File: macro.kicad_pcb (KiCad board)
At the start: 2 copper layers, 87.7 x 40.5 mm, 62 parts, among them J1 Conn_01x01_Male, J2 Conn_01x01_Male, J3 Conn_01x01_Male, Q1 BSS138, SW1 RotaryEncoder_Switch, SW2 SW_Push, U1 AP2112K-3.3, U2 W25Q128JVPIQ, U3 RP2040, Y1 12MHz

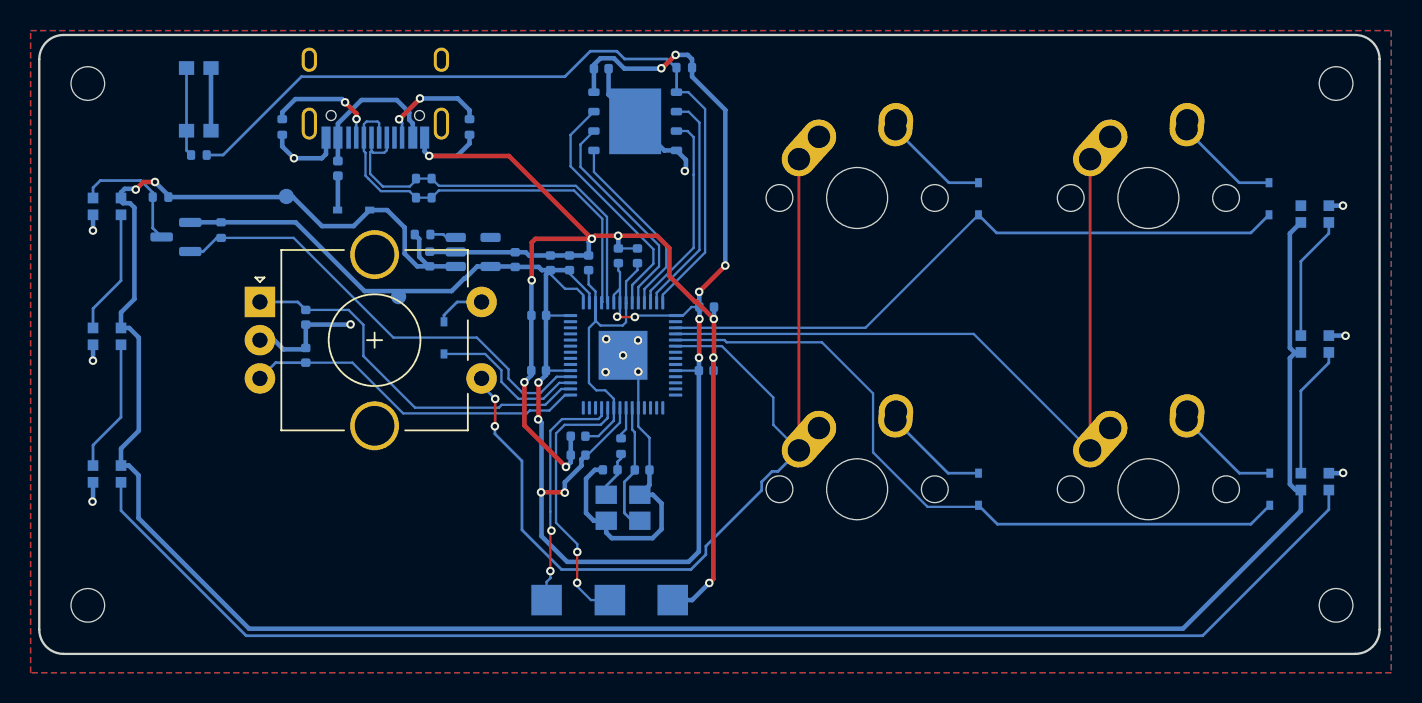
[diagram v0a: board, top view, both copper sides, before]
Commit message: Add tooling holes and logo
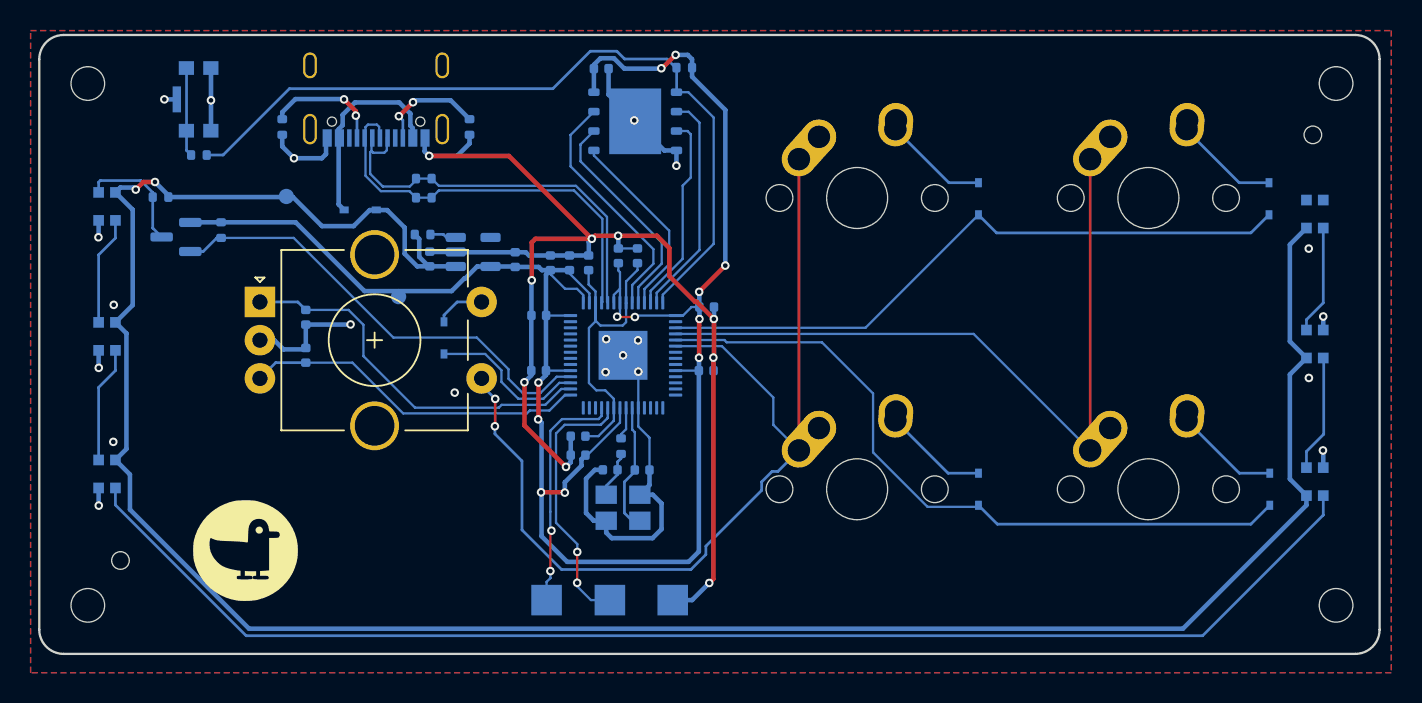
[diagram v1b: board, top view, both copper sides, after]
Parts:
- removed F1: Polyfuse, Fuse:Fuse_0402_1005Metric
- added G***: LOGO, duck:bg, F.Cu at (119.1, 111.5)
- added REF**: Tooling_Hole, MountingHole:Tooling_Hole, F.Cu at (188.9, 84.3)
- added REF**: Tooling_Hole, MountingHole:Tooling_Hole, F.Cu at (110.9, 112.2)
- SW2: footprint Button_Switch_SMD:SW_Push_1P1T_NO_CK_KMR2 -> KMR221GLFS:SW_KMR221GLFS
- USB1: footprint Type-C:HRO-TYPE-C-31-M-12-Assembly -> TYPE-C-31-M-12:HRO_TYPE-C-31-M-12
- moved USB1 4.05 mm to (127.6, 80.8)
- moved D1 0.43 mm to (126.6, 89.2)
- turned D10 to -90 degrees
- turned D11 to -90 degrees
- turned D12 to -90 degrees
- turned D7 to 90 degrees
- turned D8 to 90 degrees
- turned D9 to 90 degrees
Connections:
- D1 pad 2: Net-(D1-Pad2) -> VBUS
- D10 pad 1: +5V -> unconnected-(D10-Pad1)
- D10 pad 2: unconnected-(D10-Pad2) -> GND
- D10 pad 3: GND -> Net-(D10-Pad3)
- D10 pad 4: Net-(D10-Pad4) -> +5V
- D11 pad 1: +5V -> Net-(D10-Pad3)
- D11 pad 2: Net-(D10-Pad4) -> GND
- D11 pad 3: GND -> Net-(D11-Pad3)
- D11 pad 4: Net-(D11-Pad4) -> +5V
- D12 pad 1: +5V -> Net-(D11-Pad3)
- D12 pad 2: Net-(D11-Pad4) -> GND
- D12 pad 3: GND -> Net-(D12-Pad3)
- D12 pad 4: Net-(D12-Pad4) -> +5V
- D7 pad 1: +5V -> Net-(D7-Pad1)
- D7 pad 2: Net-(D7-Pad2) -> GND
- D7 pad 3: GND -> LED_DIN_5V
- D7 pad 4: LED_DIN_5V -> +5V
- D8 pad 1: +5V -> Net-(D8-Pad1)
- D8 pad 2: Net-(D8-Pad2) -> GND
- D8 pad 3: GND -> Net-(D7-Pad1)
- D8 pad 4: Net-(D7-Pad2) -> +5V
- D9 pad 1: +5V -> Net-(D12-Pad3)
- D9 pad 2: Net-(D12-Pad4) -> GND
- D9 pad 3: GND -> Net-(D8-Pad1)
- D9 pad 4: Net-(D8-Pad2) -> +5V
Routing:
- net Net-(D12-Pad4): track 88.9 -> 0.00 mm
- net Net-(D12-Pad3): track 0.00 -> 88.2 mm
- net Net-(D8-Pad2): track 8.66 -> 0.00 mm
- net Net-(D11-Pad4): track 8.66 -> 0.00 mm
- net Net-(D7-Pad2): track 8.16 -> 0.00 mm
- net Net-(D10-Pad4): track 8.16 -> 0.00 mm
- net Net-(D11-Pad3): track 0.00 -> 7.65 mm
- net Net-(D8-Pad1): track 0.00 -> 7.63 mm
- net Net-(D10-Pad3): track 0.00 -> 7.13 mm
- net Net-(D7-Pad1): track 0.00 -> 7.13 mm
- net VBUS: track 9.83 -> 13.2 mm
- net Net-(D1-Pad2): track 2.25 -> 0.00 mm
- net GND: track 143.3 -> 142.4 mm, vias 23 -> 30
- net +5V: track 156.2 -> 155.6 mm
- net D-: track 28.0 -> 27.5 mm
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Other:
- board text added: "+3V3"
- board text added: "JLCJLCJLCJLC"
- board text added: "Nick Yu"
- board text removed: "+3V"

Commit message: V0.1 Version
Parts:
- added G***: LOGO, duck:copper, F.Cu at (119.9, 111.8)
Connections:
- SW2 pad 5: (no net) -> GND
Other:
- board text added: "Designed by Nick Yu"
- board text added: "duckboard v0.1"
- board text removed: "Macroboard v0.1"
- board text removed: "Nick Yu"
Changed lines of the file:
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@@
   )
   (paper "A4")
+  (title_block
+    (title "duckboard")
+    (date "2023-01-07")
+    (rev "v0.1")
+    (company "Nick Yu")
+  )
   (layers
     (0 "F.Cu" signal)
@@
     (pad "" np_thru_hole circle (at 0 0) (size 1.3 1.3) (drill 1.152) (layers *.Mask))
   )
+  (footprint "duck:copper" (layer "F.Cu")
+    (at 119.88 111.82)
+    (attr board_only exclude_from_pos_files exclude_from_bom)
+    (fp_text reference "G***" (at 0 0) (layer "F.SilkS") hide
+      (effects (font (size 1.524 1.524) (thickness 0.075)))
+    )
+    (fp_text value "LOGO" (at 0.1875 0) (layer "F.SilkS") hide
+      (effects (font (size 1.524 1.524) (thickness 0.075)))
+    )
+    (fp_poly (pts
+        (xy 0.326503 1.355244)
+        (xy 0.448985 1.357604)
+        (xy 0.539347 1.362688)
+        (xy 0.602693 1.371436)
+        (xy 0.644125 1.38479)
+        (xy 0.668746 1.403692)
+        (xy 0.681658 1.429081)
+        (xy 0.686349 1.450497)
+        (xy 0.682576 1.504931)
+        (xy 0.67384 1.529292)
+        (xy 0.664298 1.541388)
+        (xy 0.646293 1.550544)
+        (xy 0.614499 1.557163)
+        (xy 0.563586 1.561645)
+        (xy 0.488225 1.564395)
+        (xy 0.383087 1.565815)
+        (xy 0.242845 1.566306)
+        (xy 0.183405 1.566334)
+        (xy 0.012613 1.565543)
+        (xy -0.118946 1.563065)
+        (xy -0.214344 1.558744)
+        (xy -0.276655 1.552422)
+        (xy -0.308951 1.543942)
+        (xy -0.313267 1.540934)
+        (xy -0.336256 1.491632)
+        (xy -0.331359 1.432012)
+        (xy -0.305405 1.387929)
+        (xy -0.288289 1.376515)
+        (xy -0.259217 1.367975)
+        (xy -0.21266 1.361919)
+        (xy -0.143092 1.357958)
+        (xy -0.044984 1.355703)
+        (xy 0.08719 1.354764)
+        (xy 0.1668 1.354667)
+      ) (layer "F.Mask") (width 0) (fill solid))
+    (fp_poly (pts
+        (xy -0.725603 1.355022)
+        (xy -0.613505 1.355729)
+        (xy -0.532323 1.357666)
+        (xy -0.476349 1.361386)
+        (xy -0.439875 1.367443)
+        (xy -0.417192 1.376391)
+        (xy -0.402592 1.388784)
+        (xy -0.392784 1.40171)
+        (xy -0.363652 1.457971)
+        (xy -0.36918 1.502578)
+        (xy -0.393095 1.533072)
+        (xy -0.425903 1.545071)
+        (xy -0.492923 1.554748)
+        (xy -0.586516 1.562089)
+        (xy -0.699047 1.567079)
+        (xy -0.822877 1.569705)
+        (xy -0.950369 1.569952)
+        (xy -1.073886 1.567808)
+        (xy -1.185791 1.563257)
+        (xy -1.278447 1.556286)
+        (xy -1.344215 1.546882)
+        (xy -1.375459 1.53503)
+        (xy -1.375605 1.534858)
+        (xy -1.389948 1.49005)
+        (xy -1.383911 1.432327)
+        (xy -1.361225 1.383573)
+        (xy -1.347697 1.371078)
+        (xy -1.319942 1.366375)
+        (xy -1.256473 1.3622)
+        (xy -1.163904 1.358779)
+        (xy -1.048854 1.356336)
+        (xy -0.917939 1.355096)
+        (xy -0.874325 1.354991)
+      ) (layer "F.Mask") (width 0) (fill solid))
+    (fp_poly (pts
+        (xy 1.014307 -1.541905)
+        (xy 1.308949 -1.534583)
+        (xy 1.363877 -1.471083)
+        (xy 1.406328 -1.39215)
+        (xy 1.413256 -1.303515)
+        (xy 1.384186 -1.219161)
+        (xy 1.373041 -1.202736)
+        (xy 1.356417 -1.183506)
+        (xy 1.3355 -1.16985)
+        (xy 1.303075 -1.160599)
+        (xy 1.251929 -1.15458)
+        (xy 1.174849 -1.150626)
+        (xy 1.064621 -1.147564)
+        (xy 1.027839 -1.14673)
+        (xy 0.719667 -1.139877)
+        (xy 0.719667 -1.549226)
+      ) (layer "F.Mask") (width 0) (fill solid))
+  )
   (footprint "MountingHole:MountingHole_2.2mm_M2" (layer "F.Cu")
     (at 190.3875 115.09375)
@@
     (property "Sheetname" "")
     (attr smd)
-    (fp_text reference "D9" (at 0 2 90) (layer "B.SilkS")
+    (fp_text reference "D9" (at -0.02 -2.02 90) (layer "B.SilkS")
       (effects (font (size 1 1) (thickness 0.15)) (justify mirror))
     )
@@
     (property "Sheetname" "")
     (attr smd)
-    (fp_text reference "D7" (at 0 2 90) (layer "B.SilkS")
+    (fp_text reference "D7" (at 0.02 -2.01 90) (layer "B.SilkS")
       (effects (font (size 1 1) (thickness 0.15)) (justify mirror))
     )
@@
     (property "Sheetname" "")
     (attr smd)
-    (fp_text reference "D8" (at 0 2 90) (layer "B.SilkS")
+    (fp_text reference "D8" (at -0.02 -1.95 90) (layer "B.SilkS")
       (effects (font (size 1 1) (thickness 0.15)) (justify mirror))
     )
@@
     (property "Sheetname" "")
     (attr smd)
-    (fp_text reference "C7" (at -2.07 0.26) (layer "B.SilkS")
+    (fp_text reference "C7" (at -1.84 0.16) (layer "B.SilkS")
       (effects (font (size 1 1) (thickness 0.15)) (justify mirror))
     )
@@
     (pad "2" smd rect (at -2.05 -0.8 270) (size 0.9 1) (layers "B.Cu" "B.Paste" "B.Mask")
       (net 1 "GND") (pinfunction "2") (pintype "passive"))
-    (pad "5" smd rect (at 0 1.425 270) (size 1.7 0.55) (layers "B.Cu" "B.Paste" "B.Mask"))
+    (pad "5" smd rect (at 0 1.425 270) (size 1.7 0.55) (layers "B.Cu" "B.Paste" "B.Mask")
+      (net 1 "GND"))
     (model "${KIPRJMOD}/KMR221GLFS/KMR221GLFS.step"
       (offset (xyz 0 0 1.5))
@@
   (gr_circle (center 148.1 96.1) (end 148.200499 96.1) (layer "B.SilkS") (width 0.15) (fill solid))
   (gr_arc (start 147.5 117) (mid 147.146447 116.853553) (end 147 116.5) (layer "B.SilkS") (width 0.15))
+  (gr_circle (center 115.19 78.87) (end 115.35 78.88) (layer "B.SilkS") (width 0.15) (fill solid))
   (gr_circle (center 141.35 107.29071) (end 141.4 107.34071) (layer "B.SilkS") (width 0.15) (fill none))
-  (gr_circle (center 116.65 90.03) (end 116.72 90.02) (layer "B.SilkS") (width 0.15) (fill none))
+  (gr_circle (center 116.67 90.04) (end 116.762195 90.04) (layer "B.SilkS") (width 0.15) (fill solid))
   (gr_circle (center 131.75 92.91) (end 131.82 92.9) (layer "B.SilkS") (width 0.15) (fill none))
   (gr_arc (start 138.896447 116.5) (mid 138.75 116.853553) (end 138.396447 117) (layer "B.SilkS") (width 0.15))
-  (gr_rect (start 118.38 113.26) (end 120.57 113.42) (layer "F.Mask") (width 0.2) (fill none))
-  (gr_rect (start 120.7025 110.21) (end 121.5875 110.7) (layer "F.Mask") (width 0.2) (fill solid))
   (gr_line (start 191.646218 77.7875) (end 107.15625 77.7875) (layer "Edge.Cuts") (width 0.15))
   (gr_line (start 191.646218 118.26875) (end 107.15625 118.26875) (layer "Edge.Cuts") (width 0.15))
@@
     (effects (font (size 1 1) (thickness 0.15)) (justify mirror))
   )
-  (gr_text "+3V3" (at 126.74 95.37) (layer "B.SilkS")
+  (gr_text "+3V3" (at 126.37 94.86) (layer "B.SilkS")
     (effects (font (size 1 1) (thickness 0.1)) (justify mirror))
   )
-  (gr_text "Macroboard v0.1" (at 168.75 114.11) (layer "B.SilkS")
-    (effects (font (size 0.508 0.508) (thickness 0.127)) (justify mirror))
+  (gr_text "duckboard v0.1" (at 168.62 113.91) (layer "B.SilkS")
+    (effects (font (size 0.81 0.81) (thickness 0.127)) (justify mirror))
   )
-  (gr_text "+5V" (at 119.53 87.5) (layer "B.SilkS")
+  (gr_text "+5V" (at 119.34 88.32) (layer "B.SilkS")
     (effects (font (size 1 1) (thickness 0.1)) (justify mirror))
   )
-  (gr_text "JLCJLCJLCJLC" (at 186.17 117.29) (layer "B.SilkS")
-    (effects (font (size 0.508 0.508) (thickness 0.127)) (justify mirror))
+  (gr_text "JLCJLCJLCJLC" (at 185.26 117.25) (layer "B.SilkS")
+    (effects (font (size 0.81 0.8) (thickness 0.127)) (justify mirror))
   )
   (gr_text "SWD" (at 136.5 117) (layer "B.SilkS")
     (effects (font (size 1 1) (thickness 0.15)) (justify mirror))
   )
-  (gr_text "Nick Yu" (at 168.76 115.12) (layer "B.SilkS")
+  (gr_text "Designed by Nick Yu" (at 168.76 115.12) (layer "B.SilkS")
     (effects (font (size 0.508 0.508) (thickness 0.127)) (justify mirror))
   )
